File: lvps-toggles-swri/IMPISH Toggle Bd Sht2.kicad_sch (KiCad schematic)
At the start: 8 parts, among them J1 MTSW-117-12-L-D-840, J2 BCS-110-L-D-TE

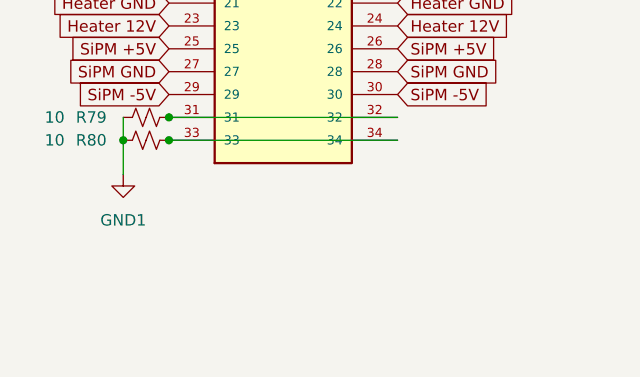
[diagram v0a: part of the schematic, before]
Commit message: toggles adapter board
The SwRI toggle output is in the wrong direction,
so we are adding an additional PCB to point the power
towards the side of the EPS box. We can route it with
cables and connectors instead of using the board-to-board
style interface.
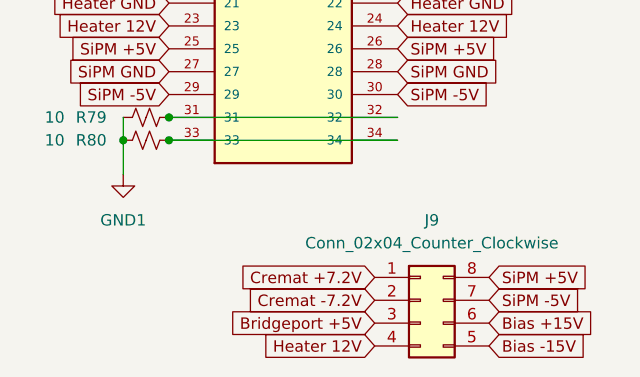
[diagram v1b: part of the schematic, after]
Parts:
- added J9: Conn_02x04_Counter_Clockwise, Connector_PinSocket_2.54mm:PinSocket_2x04_P2.54mm_Vertical, symbol Connector_Generic:Conn_02x04_Counter_Clockwise
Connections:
- net Bias +15V: now also J9.6 (Pin_6)
- net Bias -15V: now also J9.5 (Pin_5)
- net Bridgeport +5V: now also J9.3 (Pin_3)
- net Cremat +7.2V: now also J9.1 (Pin_1)
- net Cremat -7.2V: now also J9.2 (Pin_2)
- net Heater 12V: now also J9.4 (Pin_4)
- net SiPM +5V: now also J9.8 (Pin_8)
- net SiPM -5V: now also J9.7 (Pin_7)

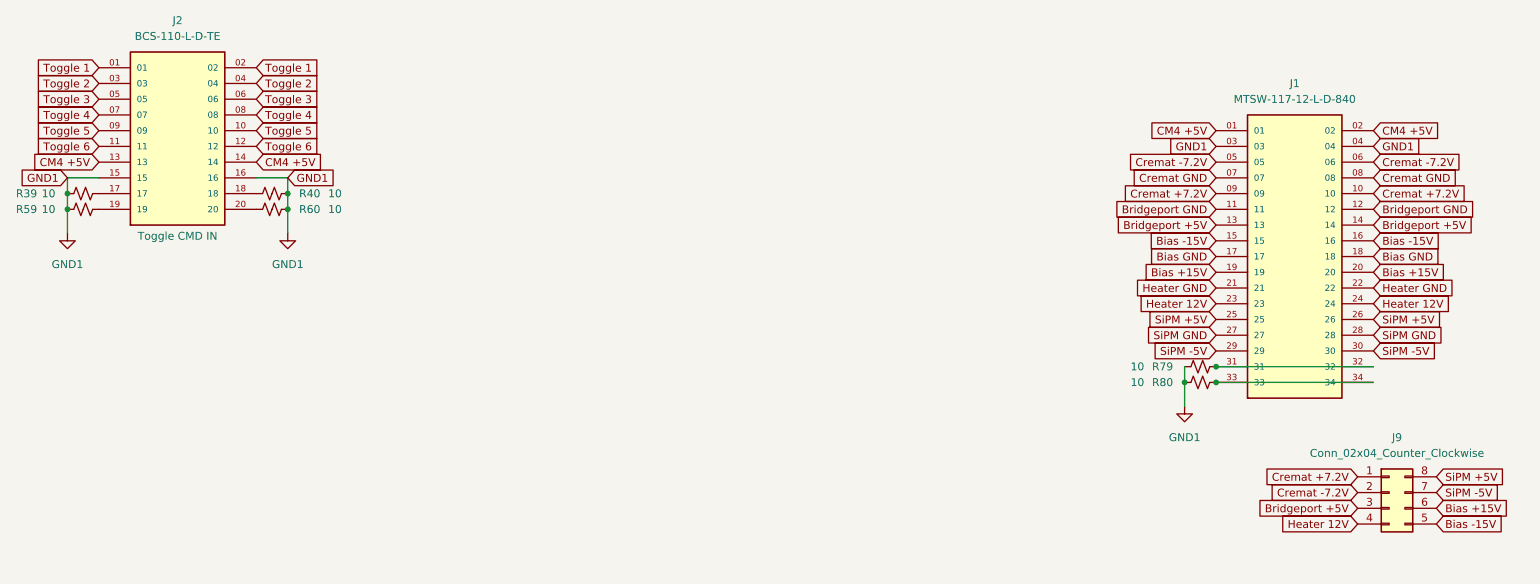
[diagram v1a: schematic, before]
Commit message: swri toggles: start one ground
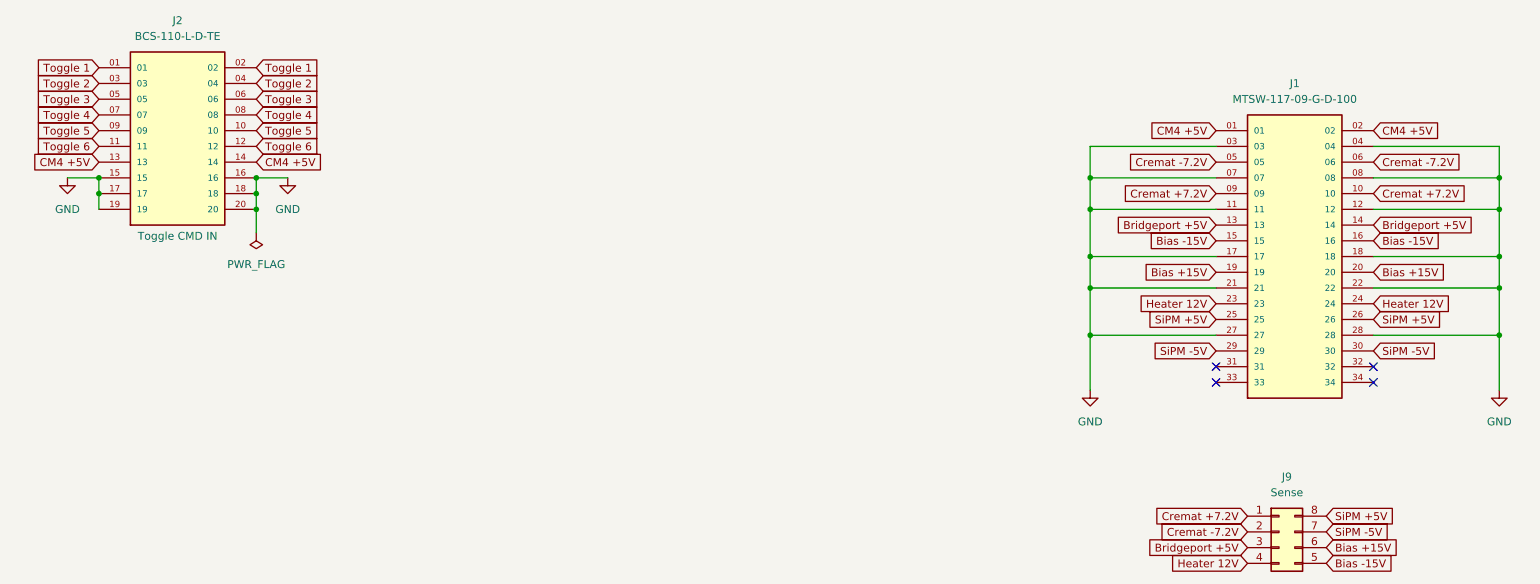
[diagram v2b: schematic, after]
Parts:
- removed R39, R40, R59, R60, R79, R80: 10, Resistor_SMD:R_0805_2012Metric_Pad1.20x1.40mm_HandSolder, symbol Device:R_Small_US
- J1: value MTSW-117-12-L-D-840 -> MTSW-117-09-G-D-100
- J9: value Conn_02x04_Counter_Clockwise -> Sense
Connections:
- net Bias GND is gone; now on net GND: J1.17, J1.18
- net Bridgeport GND is gone; now on net GND: J1.11, J1.12
- net Cremat GND is gone; now on net GND: J1.07, J1.08
- net GND1 is gone; now on net GND: J1.03, J1.04, J2.15, J2.16
- net Heater GND is gone; now on net GND: J1.21, J1.22
- net SiPM GND is gone; now on net GND: J1.27, J1.28
- net at J1.31: no longer J1.32
- net at J1.33: no longer J1.34
- net GND: now reaches J2.20
- net GND: now also J2.17, J2.18, J2.19
- no-connect marks 0 -> 4
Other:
- moved on the sheet: J9
